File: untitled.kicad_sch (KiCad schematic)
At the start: 17 parts, among them J1 Conn_01x06, J10 Conn_01x06, J11 Conn_01x06, J12 Conn_01x06, J13 Conn_01x06, J14 Conn_01x06, J15 Conn_01x06, J2 Conn_01x06, J3 Conn_01x06, J4 Conn_01x06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

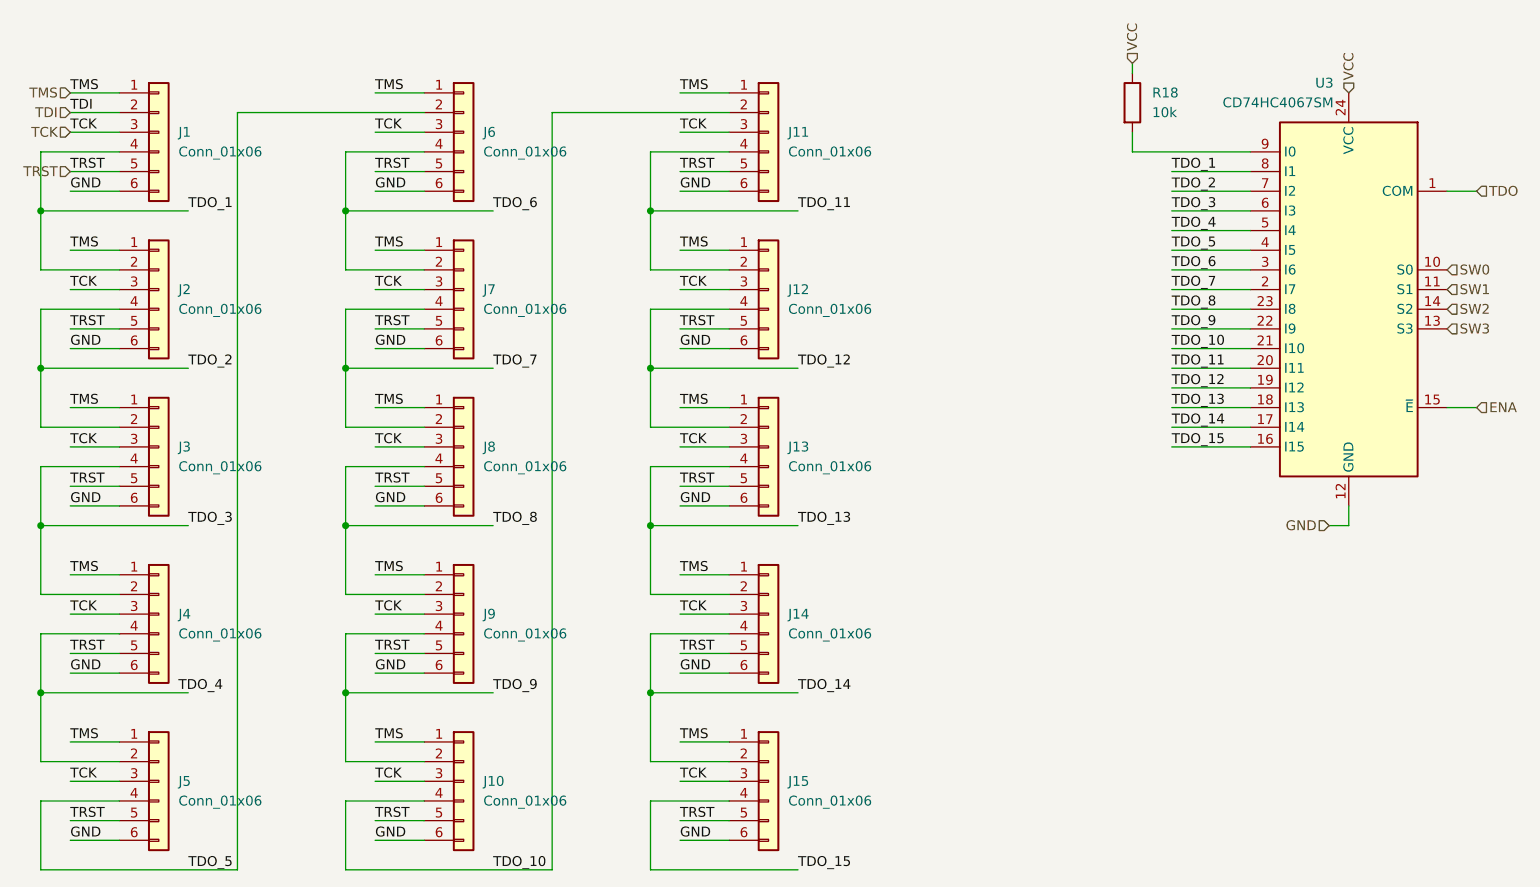
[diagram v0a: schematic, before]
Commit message: change dip switch type, change reset position
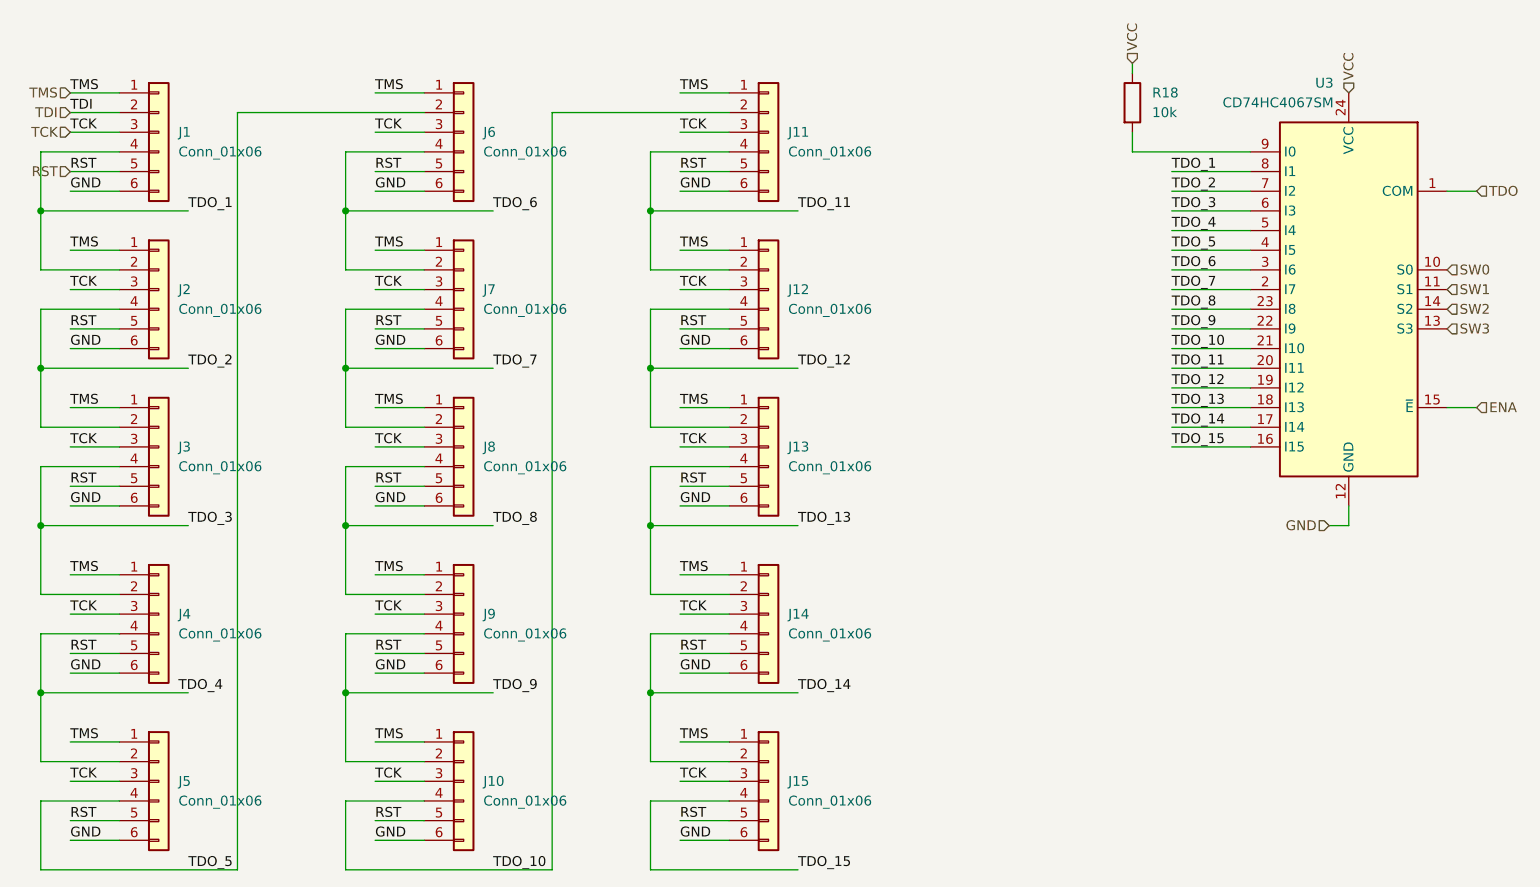
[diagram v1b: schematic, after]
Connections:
- net TRST renamed RST
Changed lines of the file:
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@@
     (effects (font (size 1.27 1.27)) (justify left bottom))
   )
-  (label "TRST" (at 72.39 78.74 0) (fields_autoplaced)
-    (effects (font (size 1.27 1.27)) (justify left bottom))
-  )
-  (label "TRST" (at 72.39 100.33 0) (fields_autoplaced)
+  (label "RST" (at 72.39 78.74 0) (fields_autoplaced)
+    (effects (font (size 1.27 1.27)) (justify left bottom))
+  )
+  (label "RST" (at 72.39 100.33 0) (fields_autoplaced)
     (effects (font (size 1.27 1.27)) (justify left bottom))
   )
@@
     (effects (font (size 1.27 1.27)) (justify left bottom))
   )
-  (label "TRST" (at 111.76 58.42 0) (fields_autoplaced)
+  (label "RST" (at 111.76 58.42 0) (fields_autoplaced)
     (effects (font (size 1.27 1.27)) (justify left bottom))
   )
@@
     (effects (font (size 1.27 1.27)) (justify left bottom))
   )
-  (label "TRST" (at 72.39 38.1 0) (fields_autoplaced)
+  (label "RST" (at 72.39 38.1 0) (fields_autoplaced)
     (effects (font (size 1.27 1.27)) (justify left bottom))
   )
@@
     (effects (font (size 1.27 1.27)) (justify left bottom))
   )
-  (label "TRST" (at 72.39 58.42 0) (fields_autoplaced)
+  (label "RST" (at 72.39 58.42 0) (fields_autoplaced)
     (effects (font (size 1.27 1.27)) (justify left bottom))
   )
@@
     (effects (font (size 1.27 1.27)) (justify left bottom))
   )
-  (label "TRST" (at 33.02 78.74 0) (fields_autoplaced)
+  (label "RST" (at 33.02 78.74 0) (fields_autoplaced)
     (effects (font (size 1.27 1.27)) (justify left bottom))
   )
@@
     (effects (font (size 1.27 1.27)) (justify left bottom))
   )
-  (label "TRST" (at 33.02 58.42 0) (fields_autoplaced)
+  (label "RST" (at 33.02 58.42 0) (fields_autoplaced)
     (effects (font (size 1.27 1.27)) (justify left bottom))
   )
@@
     (effects (font (size 1.27 1.27)) (justify left bottom))
   )
-  (label "TRST" (at 33.02 100.33 0) (fields_autoplaced)
+  (label "RST" (at 33.02 100.33 0) (fields_autoplaced)
     (effects (font (size 1.27 1.27)) (justify left bottom))
   )
@@
     (effects (font (size 1.27 1.27)) (justify left bottom))
   )
-  (label "TRST" (at 111.76 100.33 0) (fields_autoplaced)
+  (label "RST" (at 111.76 100.33 0) (fields_autoplaced)
     (effects (font (size 1.27 1.27)) (justify left bottom))
   )
@@
     (effects (font (size 1.27 1.27)) (justify left bottom))
   )
-  (label "TRST" (at 111.76 121.92 0) (fields_autoplaced)
+  (label "RST" (at 111.76 121.92 0) (fields_autoplaced)
     (effects (font (size 1.27 1.27)) (justify left bottom))
   )
@@
     (effects (font (size 1.27 1.27)) (justify left bottom))
   )
-  (label "TRST" (at 33.02 38.1 0) (fields_autoplaced)
+  (label "RST" (at 33.02 38.1 0) (fields_autoplaced)
     (effects (font (size 1.27 1.27)) (justify left bottom))
   )
@@
     (effects (font (size 1.27 1.27)) (justify left bottom))
   )
-  (label "TRST" (at 111.76 78.74 0) (fields_autoplaced)
+  (label "RST" (at 111.76 78.74 0) (fields_autoplaced)
     (effects (font (size 1.27 1.27)) (justify left bottom))
   )
@@
     (effects (font (size 1.27 1.27)) (justify left bottom))
   )
-  (label "TRST" (at 111.76 38.1 0) (fields_autoplaced)
+  (label "RST" (at 111.76 38.1 0) (fields_autoplaced)
     (effects (font (size 1.27 1.27)) (justify left bottom))
   )
@@
     (effects (font (size 1.27 1.27)) (justify left bottom))
   )
-  (label "TRST" (at 33.02 121.92 0) (fields_autoplaced)
+  (label "RST" (at 33.02 121.92 0) (fields_autoplaced)
     (effects (font (size 1.27 1.27)) (justify left bottom))
   )
@@
     (effects (font (size 1.27 1.27)) (justify left bottom))
   )
-  (label "TRST" (at 72.39 121.92 0) (fields_autoplaced)
+  (label "RST" (at 72.39 121.92 0) (fields_autoplaced)
     (effects (font (size 1.27 1.27)) (justify left bottom))
   )
@@
     (effects (font (size 1.27 1.27)) (justify right))
   )
-  (hierarchical_label "TRST" (shape input) (at 33.02 38.1 180) (fields_autoplaced)
-    (effects (font (size 1.27 1.27)) (justify right))
-  )
+  (hierarchical_label "RST" (shape input) (at 33.02 38.1 180) (fields_autoplaced)
+    (effects (font (size 1.27 1.27)) (justify right))
+  )
